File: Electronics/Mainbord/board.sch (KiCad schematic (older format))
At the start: 54 parts, among them J16 Screw_Terminal_01x10, J17 Screw_Terminal_01x10, J18 Screw_Terminal_01x10, J19 Screw_Terminal_01x10, J20 Screw_Terminal_01x10, J21 Screw_Terminal_01x10, J22 Screw_Terminal_01x10, J23 Screw_Terminal_01x10, J24 Screw_Terminal_01x10, J25 Screw_Terminal_01x10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

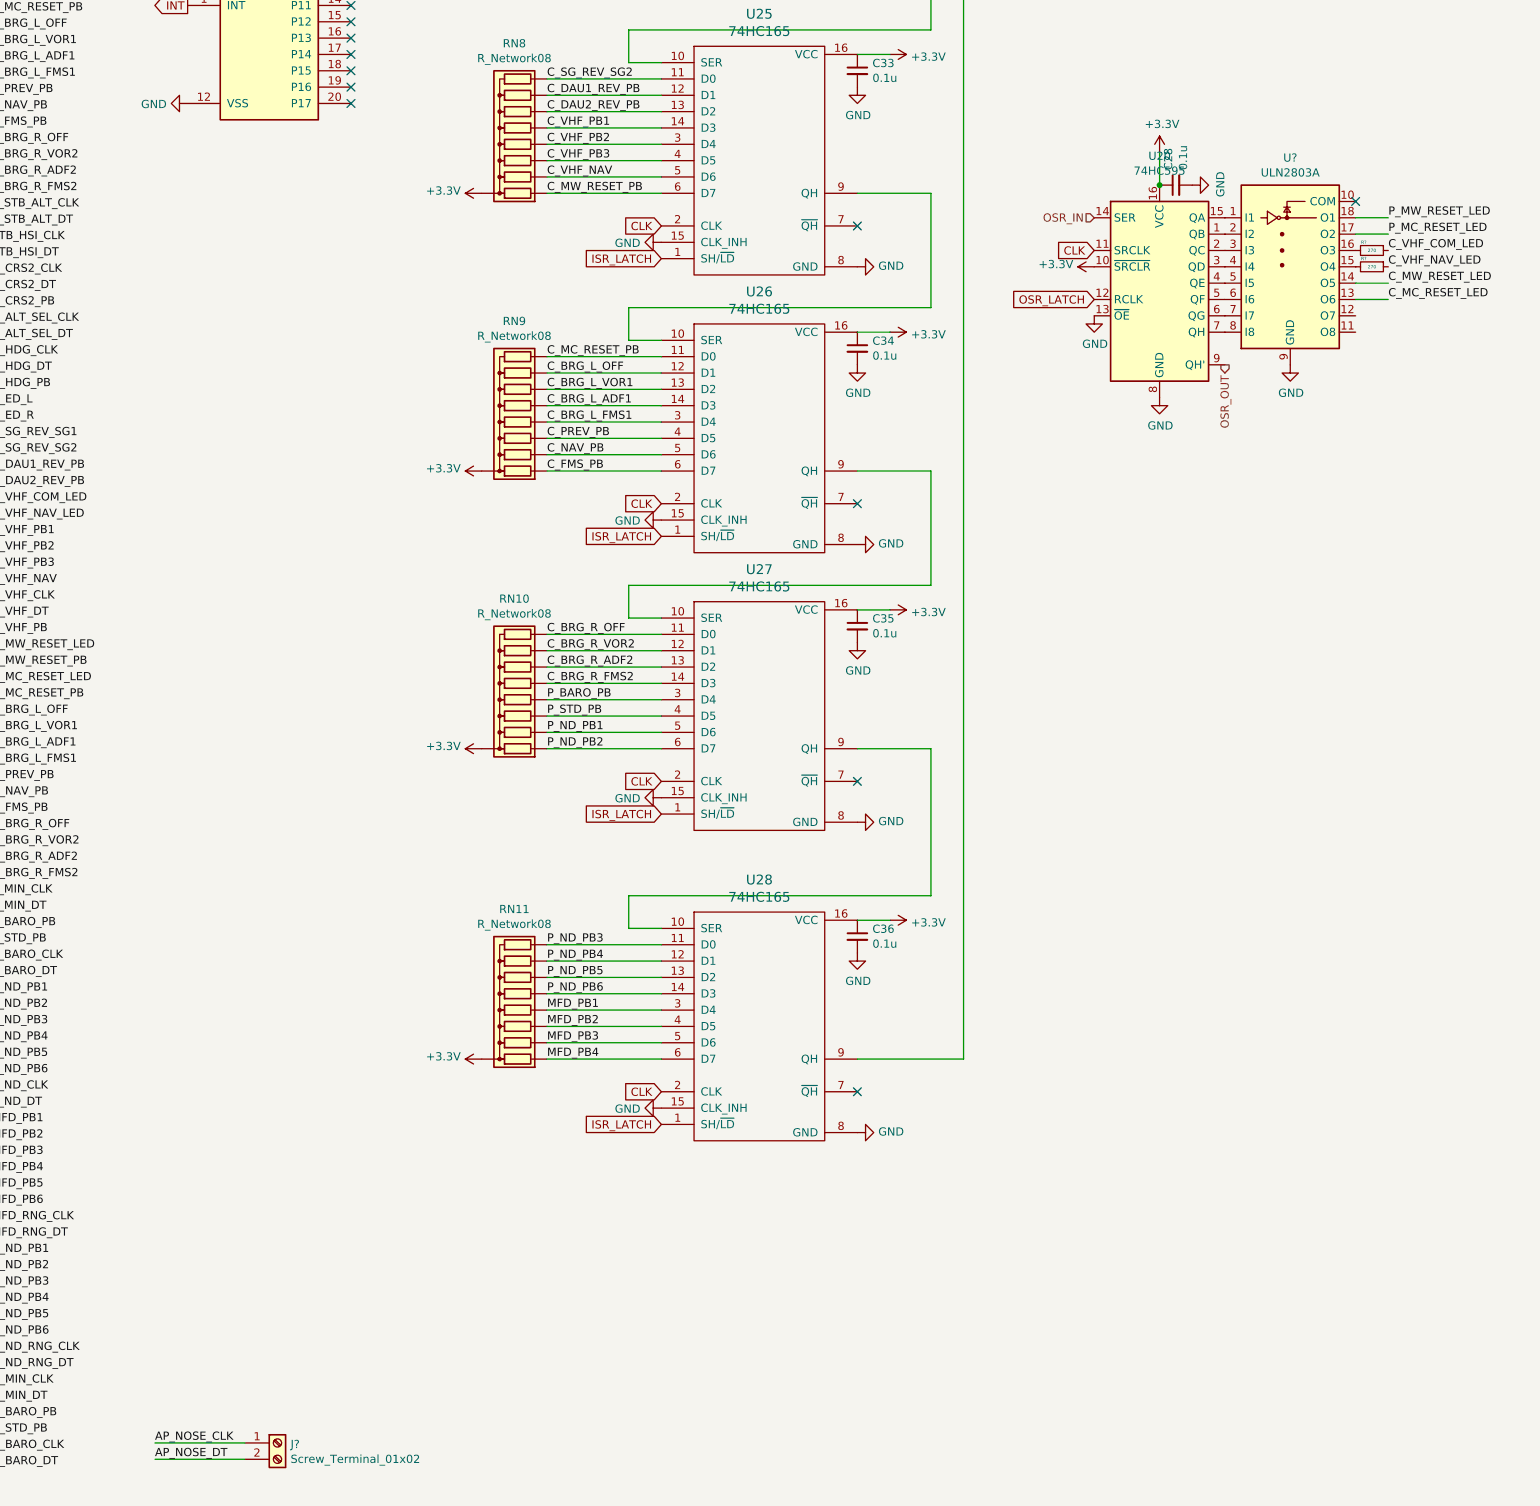
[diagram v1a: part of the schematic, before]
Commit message: Electronics - Minor changes
Resistors to LEDs, transistors
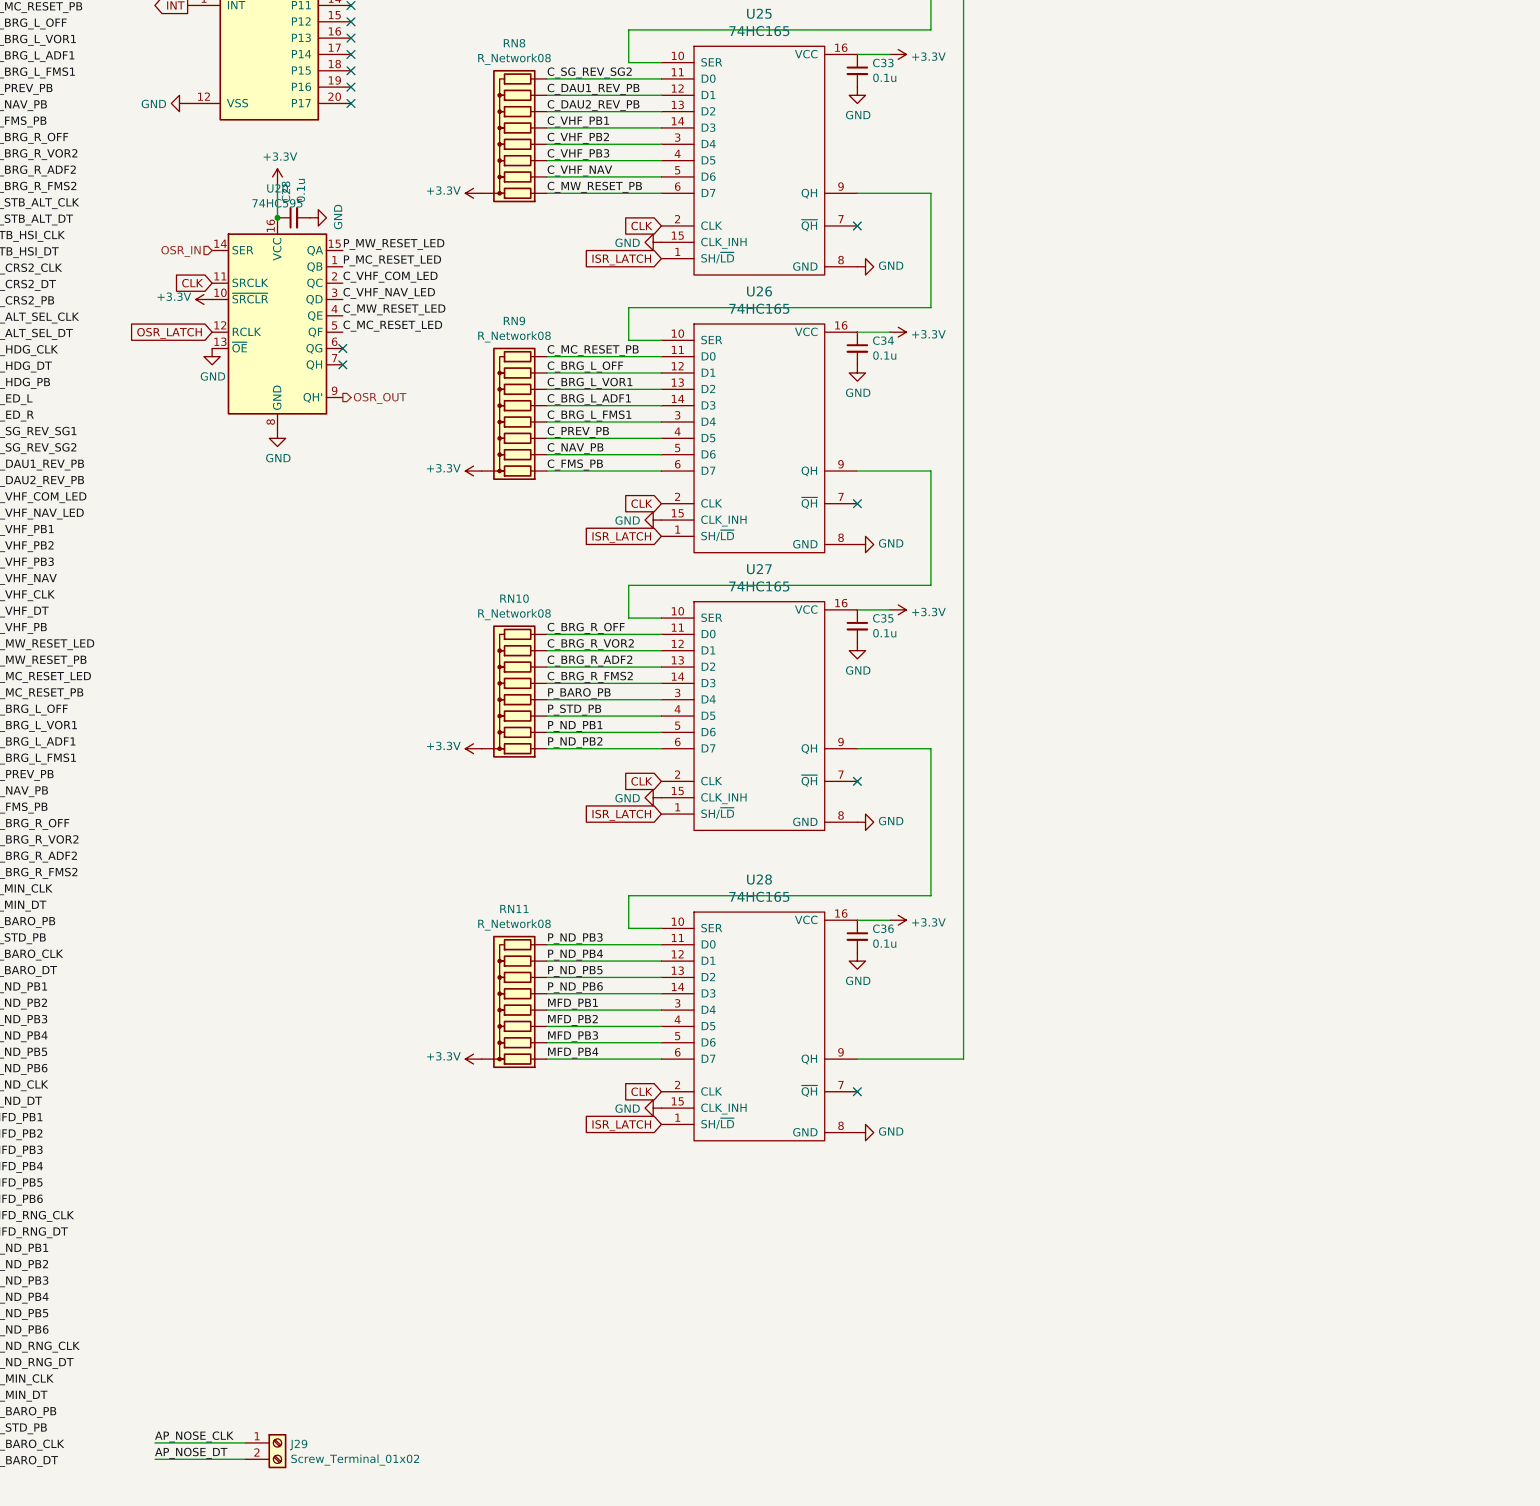
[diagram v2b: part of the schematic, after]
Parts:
- removed R? (x2): 270, symbol Device:R_Small
- removed U?: ULN2803A, symbol Transistor_Array:ULN2803A
- gave numbers to parts that had none: 1
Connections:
- net C_MC_RESET_LED: now also U20.5 (QF)
- net C_MW_RESET_LED: now also U20.4 (QE)
- net C_VHF_COM_LED: now also U20.2 (QC)
- net C_VHF_NAV_LED: now also U20.3 (QD)
- net P_MC_RESET_LED: now also U20.1 (QB)
- net P_MW_RESET_LED: now also U20.15 (QA)
- no-connect marks 34 -> 35
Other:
- moved on the sheet: C28, U20
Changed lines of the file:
@@
 EESchema Schematic File Version 4
-EELAYER 30 0
+LIBS:Mainboard-cache
+EELAYER 26 0
 EELAYER END
 $Descr A3 11693 16535 portrait
@@
 L Device:C_Small C?
 U 1 1 5DF1ADB9
-P 9000 8050
+P 3600 8250
 AR Path="/5DB5DCD1/5DF1ADB9" Ref="C?"  Part="1"
 AR Path="/5DC174D4/5DF1ADB9" Ref="C?"  Part="1"
 AR Path="/5DB6029E/5DF1ADB9" Ref="C28"  Part="1"
-F 0 "C28" H 9092 8096 50  0000 L CNN
-F 1 "0.1u" H 9092 8005 50  0000 L CNN
-F 2 "" H 9000 8050 50  0001 C CNN
-F 3 "~" H 9000 8050 50  0001 C CNN
-	1    9000 8050
+F 0 "C28" H 3692 8296 50  0000 L CNN
+F 1 "0.1u" H 3692 8205 50  0000 L CNN
+F 2 "" H 3600 8250 50  0001 C CNN
+F 3 "~" H 3600 8250 50  0001 C CNN
+	1    3600 8250
 	0    -1   -1   0
 $EndComp
@@
 L power:GND #PWR?
 U 1 1 5DF1ADC0
-P 9100 8050
+P 3700 8250
 AR Path="/5DB5DCD1/5DF1ADC0" Ref="#PWR?"  Part="1"
 AR Path="/5DC174D4/5DF1ADC0" Ref="#PWR?"  Part="1"
 AR Path="/5DB6029E/5DF1ADC0" Ref="#PWR0245"  Part="1"
-F 0 "#PWR0245" H 9100 7800 50  0001 C CNN
-F 1 "GND" H 9105 7877 50  0000 C CNN
-F 2 "" H 9100 8050 50  0001 C CNN
-F 3 "" H 9100 8050 50  0001 C CNN
-	1    9100 8050
-	0    -1   -1   0
-$EndComp
-Wire Wire Line
-	8900 8050 8900 7850
+F 0 "#PWR0245" H 3700 8000 50  0001 C CNN
+F 1 "GND" H 3705 8077 50  0000 C CNN
+F 2 "" H 3700 8250 50  0001 C CNN
+F 3 "" H 3700 8250 50  0001 C CNN
+	1    3700 8250
+	0    -1   -1   0
+$EndComp
+Wire Wire Line
+	3500 8250 3500 8050
 $Comp
 L 74xx:74HC595 U?
 U 1 1 5DF1ADC7
-P 8900 8650
+P 3500 8850
 AR Path="/5DB5DCD1/5DF1ADC7" Ref="U?"  Part="1"
 AR Path="/5DC174D4/5DF1ADC7" Ref="U?"  Part="1"
 AR Path="/5DB6029E/5DF1ADC7" Ref="U20"  Part="1"
-F 0 "U20" H 8900 9428 50  0000 C CNN
-F 1 "74HC595" H 8900 9337 50  0000 C CNN
-F 2 "" H 8900 8650 50  0001 C CNN
-F 3 "http://www.ti.com/lit/ds/symlink/sn74hc595.pdf" H 8900 8650 50  0001 C CNN
-	1    8900 8650
-	1    0    0    -1
-$EndComp
-Connection ~ 8900 8050
+F 0 "U20" H 3500 9628 50  0000 C CNN
+F 1 "74HC595" H 3500 9537 50  0000 C CNN
+F 2 "" H 3500 8850 50  0001 C CNN
+F 3 "http://www.ti.com/lit/ds/symlink/sn74hc595.pdf" H 3500 8850 50  0001 C CNN
+	1    3500 8850
+	1    0    0    -1
+$EndComp
+Connection ~ 3500 8250
 $Comp
 L power:GND #PWR?
 U 1 1 5DF1ADCF
-P 8900 9350
+P 3500 9550
 AR Path="/5DB5DCD1/5DF1ADCF" Ref="#PWR?"  Part="1"
 AR Path="/5DC174D4/5DF1ADCF" Ref="#PWR?"  Part="1"
 AR Path="/5DB6029E/5DF1ADCF" Ref="#PWR0246"  Part="1"
-F 0 "#PWR0246" H 8900 9100 50  0001 C CNN
-F 1 "GND" H 8905 9177 50  0000 C CNN
-F 2 "" H 8900 9350 50  0001 C CNN
-F 3 "" H 8900 9350 50  0001 C CNN
-	1    8900 9350
-	1    0    0    -1
-$EndComp
-Text HLabel 8500 8250 0    50   Input ~ 0
+F 0 "#PWR0246" H 3500 9300 50  0001 C CNN
+F 1 "GND" H 3505 9377 50  0000 C CNN
+F 2 "" H 3500 9550 50  0001 C CNN
+F 3 "" H 3500 9550 50  0001 C CNN
+	1    3500 9550
+	1    0    0    -1
+$EndComp
+Text HLabel 3100 8450 0    50   Input ~ 0
 OSR_IN
 $Comp
 L power:GND #PWR?
 U 1 1 5DF1ADD6
-P 8500 8850
+P 3100 9050
 AR Path="/5DB5DCD1/5DF1ADD6" Ref="#PWR?"  Part="1"
 AR Path="/5DC174D4/5DF1ADD6" Ref="#PWR?"  Part="1"
 AR Path="/5DB6029E/5DF1ADD6" Ref="#PWR0247"  Part="1"
-F 0 "#PWR0247" H 8500 8600 50  0001 C CNN
-F 1 "GND" H 8505 8677 50  0000 C CNN
-F 2 "" H 8500 8850 50  0001 C CNN
-F 3 "" H 8500 8850 50  0001 C CNN
-	1    8500 8850
+F 0 "#PWR0247" H 3100 8800 50  0001 C CNN
+F 1 "GND" H 3105 8877 50  0000 C CNN
+F 2 "" H 3100 9050 50  0001 C CNN
+F 3 "" H 3100 9050 50  0001 C CNN
+	1    3100 9050
 	1    0    0    -1
 $EndComp
@@
 L power:+3.3V #PWR?
 U 1 1 5DF1ADDD
-P 8900 7850
+P 3500 8050
 AR Path="/5DB5DCD1/5DF1ADDD" Ref="#PWR?"  Part="1"
 AR Path="/5DC174D4/5DF1ADDD" Ref="#PWR?"  Part="1"
 AR Path="/5DB6029E/5DF1ADDD" Ref="#PWR0248"  Part="1"
-F 0 "#PWR0248" H 8900 7700 50  0001 C CNN
-F 1 "+3.3V" H 8915 8023 50  0000 C CNN
-F 2 "" H 8900 7850 50  0001 C CNN
-F 3 "" H 8900 7850 50  0001 C CNN
-	1    8900 7850
+F 0 "#PWR0248" H 3500 7900 50  0001 C CNN
+F 1 "+3.3V" H 3515 8223 50  0000 C CNN
+F 2 "" H 3500 8050 50  0001 C CNN
+F 3 "" H 3500 8050 50  0001 C CNN
+	1    3500 8050
 	1    0    0    -1
 $EndComp
@@
 L power:+3.3V #PWR?
 U 1 1 5DF1ADE3
-P 8500 8550
+P 3100 8750
 AR Path="/5DB5DCD1/5DF1ADE3" Ref="#PWR?"  Part="1"
 AR Path="/5DC174D4/5DF1ADE3" Ref="#PWR?"  Part="1"
 AR Path="/5DB6029E/5DF1ADE3" Ref="#PWR0249"  Part="1"
-F 0 "#PWR0249" H 8500 8400 50  0001 C CNN
-F 1 "+3.3V" V 8515 8678 50  0000 L CNN
-F 2 "" H 8500 8550 50  0001 C CNN
-F 3 "" H 8500 8550 50  0001 C CNN
-	1    8500 8550
-	0    -1   -1   0
-$EndComp
-Text GLabel 8500 8450 0    50   Input ~ 0
+F 0 "#PWR0249" H 3100 8600 50  0001 C CNN
+F 1 "+3.3V" V 3115 8878 50  0000 L CNN
+F 2 "" H 3100 8750 50  0001 C CNN
+F 3 "" H 3100 8750 50  0001 C CNN
+	1    3100 8750
+	0    -1   -1   0
+$EndComp
+Text GLabel 3100 8650 0    50   Input ~ 0
 CLK
+Text Label 3900 8450 0    50   ~ 0
+P_MW_RESET_LED
 Text Label 5150 4000 0    50   ~ 0
 P_MW_RESET_PB
+Text Label 3900 8550 0    50   ~ 0
+P_MC_RESET_LED
 Text Label 5150 4100 0    50   ~ 0
 P_MC_RESET_PB
@@
 Text Label 4000 4550 0    50   ~ 0
 C_VHF_PB
+Text Label 3900 8850 0    50   ~ 0
+C_MW_RESET_LED
 Text Label 5150 8100 0    50   ~ 0
 C_MW_RESET_PB
+Text Label 3900 8950 0    50   ~ 0
+C_MC_RESET_LED
 Text Label 5150 9100 0    50   ~ 0
 C_MC_RESET_PB
@@
 Text Label 4000 4750 0    50   ~ 0
 P_MIN_DT
+Text Label 3900 8650 0    50   ~ 0
+C_VHF_COM_LED
+Text Label 3900 8750 0    50   ~ 0
+C_VHF_NAV_LED
 Text Label 1750 12700 0    50   ~ 0
 P_STD_PB
@@
 Text Label 1750 15900 0    50   ~ 0
 C_BARO_DT
-Text HLabel 9300 9150 3    50   Output ~ 0
+Text HLabel 3900 9350 2    50   Output ~ 0
 OSR_OUT
 $Comp
@@
 Wire Wire Line
 	5150 11000 5850 11000
+NoConn ~ 3900 9050
+NoConn ~ 3900 9150
 NoConn ~ 1950 5500
 NoConn ~ 3950 6650
@@
 P 3500 15750
 AR Path="/5DC33C09/5DDEDB63" Ref="J?"  Part="1"
-AR Path="/5DB6029E/5DDEDB63" Ref="J?"  Part="1"
-F 0 "J?" H 3580 15742 50  0000 L CNN
+AR Path="/5DB6029E/5DDEDB63" Ref="J29"  Part="1"
+F 0 "J29" H 3580 15742 50  0000 L CNN
 F 1 "Screw_Terminal_01x02" H 3580 15651 50  0000 L CNN
 F 2 "" H 3500 15750 50  0001 C CNN
@@
 Text GLabel 2950 6950 0    50   Output ~ 0
 INT
-Text GLabel 8500 8750 0    50   Input ~ 0
+Text GLabel 3100 8950 0    50   Input ~ 0
 OSR_LATCH
-$Comp
-L Transistor_Array:ULN2803A U?
-U 1 1 5DF8E5E4
-P 9700 8450
-F 0 "U?" H 9700 9017 50  0000 C CNN
-F 1 "ULN2803A" H 9700 8926 50  0000 C CNN
-F 2 "" H 9750 7800 50  0001 L CNN
-F 3 "http://www.ti.com/lit/ds/symlink/uln2803a.pdf" H 9800 8250 50  0001 C CNN
-	1    9700 8450
-	1    0    0    -1
-$EndComp
-$Comp
-L power:GND #PWR?
-U 1 1 5DF90A33
-P 9700 9150
-AR Path="/5DB5DCD1/5DF90A33" Ref="#PWR?"  Part="1"
-AR Path="/5DC174D4/5DF90A33" Ref="#PWR?"  Part="1"
-AR Path="/5DB6029E/5DF90A33" Ref="#PWR?"  Part="1"
-F 0 "#PWR?" H 9700 8900 50  0001 C CNN
-F 1 "GND" H 9705 8977 50  0000 C CNN
-F 2 "" H 9700 9150 50  0001 C CNN
-F 3 "" H 9700 9150 50  0001 C CNN
-	1    9700 9150
-	1    0    0    -1
-$EndComp
-$Comp
-L Device:R_Small R?
-U 1 1 5DFBCA65
-P 10200 8450
-AR Path="/5DC33C09/5DFBCA65" Ref="R?"  Part="1"
-AR Path="/5DB6029E/5DFBCA65" Ref="R?"  Part="1"
-F 0 "R?" V 10150 8400 20  0000 C CNN
-F 1 "270" V 10200 8450 20  0000 C CNN
-F 2 "" H 10200 8450 50  0001 C CNN
-F 3 "~" H 10200 8450 50  0001 C CNN
-	1    10200 8450
-	0    1    1    0
-$EndComp
-Text Label 10300 8550 0    50   ~ 0
-C_VHF_NAV_LED
-Text Label 10300 8450 0    50   ~ 0
-C_VHF_COM_LED
-Text Label 10300 8750 0    50   ~ 0
-C_MC_RESET_LED
-Text Label 10300 8650 0    50   ~ 0
-C_MW_RESET_LED
-Text Label 10300 8350 0    50   ~ 0
-P_MC_RESET_LED
-Text Label 10300 8250 0    50   ~ 0
-P_MW_RESET_LED
-$Comp
-L Device:R_Small R?
-U 1 1 5DFE47EA
-P 10200 8550
-AR Path="/5DC33C09/5DFE47EA" Ref="R?"  Part="1"
-AR Path="/5DB6029E/5DFE47EA" Ref="R?"  Part="1"
-F 0 "R?" V 10150 8500 20  0000 C CNN
-F 1 "270" V 10200 8550 20  0000 C CNN
-F 2 "" H 10200 8550 50  0001 C CNN
-F 3 "~" H 10200 8550 50  0001 C CNN
-	1    10200 8550
-	0    1    1    0
-$EndComp
-Wire Wire Line
-	10100 8650 10300 8650
-Wire Wire Line
-	10300 8750 10100 8750
-Wire Wire Line
-	10100 8350 10300 8350
-Wire Wire Line
-	10300 8250 10100 8250
-NoConn ~ 10100 8150
 $EndSCHEMATC
